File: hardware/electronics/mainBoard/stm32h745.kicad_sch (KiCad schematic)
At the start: 58 parts, among them SW1 PTS810, SW2 PTS810, U1 STM32H745ZIT6, U2 TCAN3403-Q1

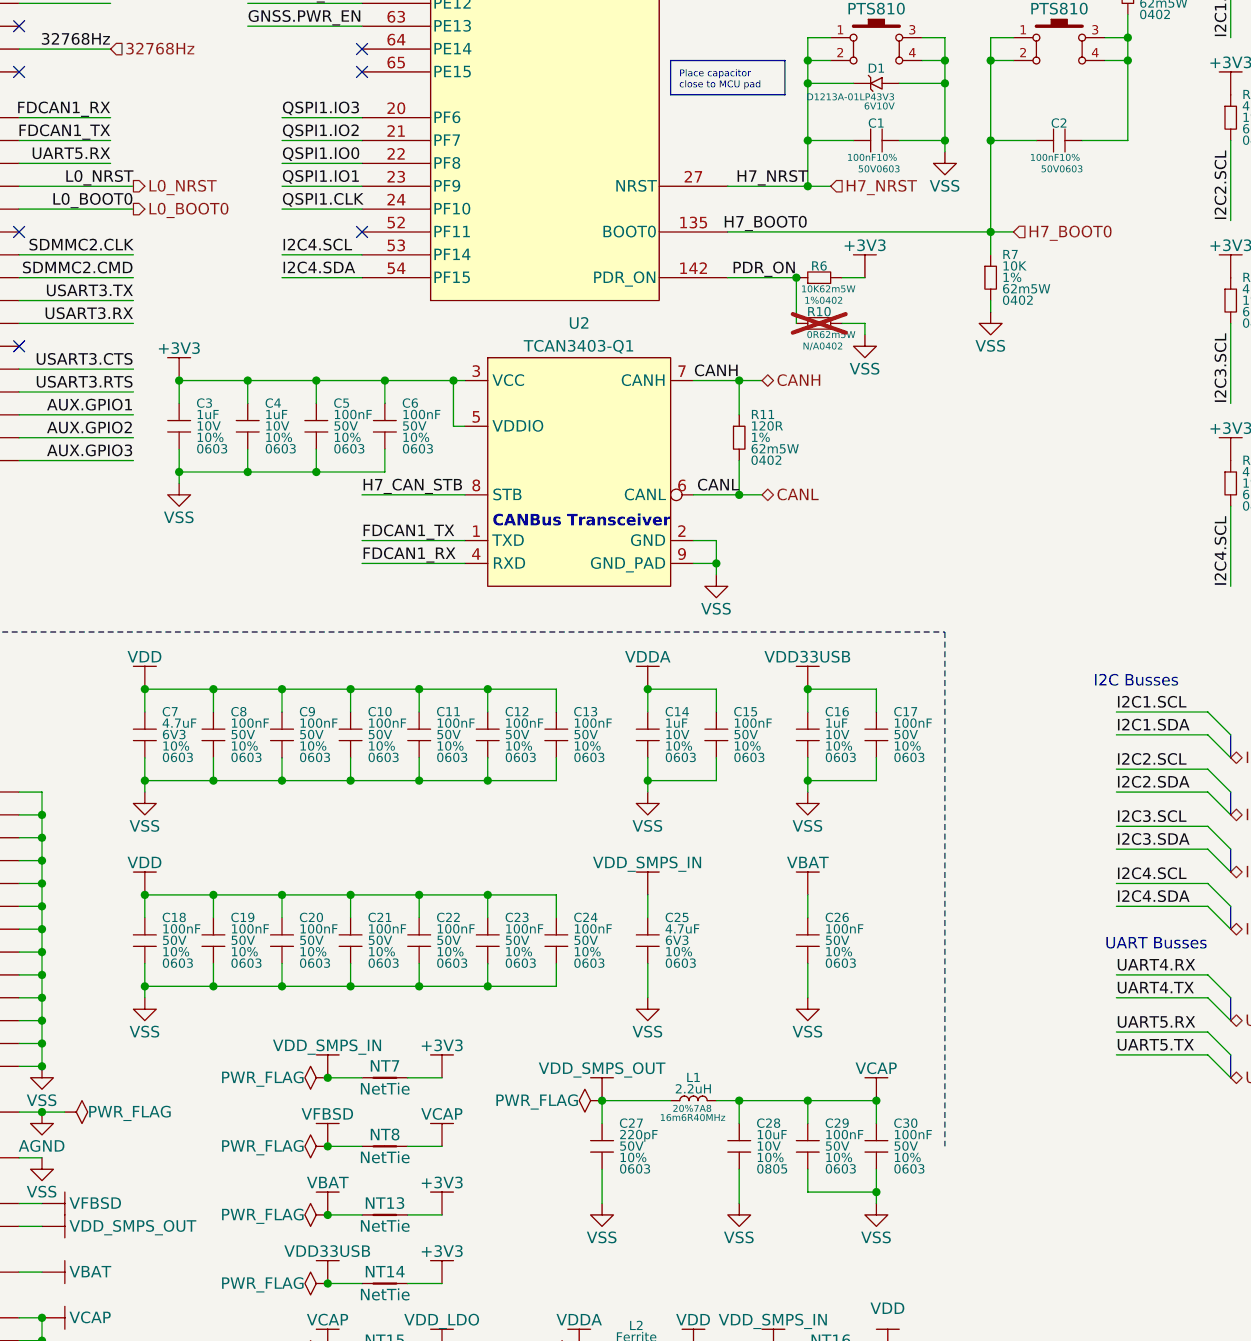
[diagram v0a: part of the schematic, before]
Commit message: updated capacitors
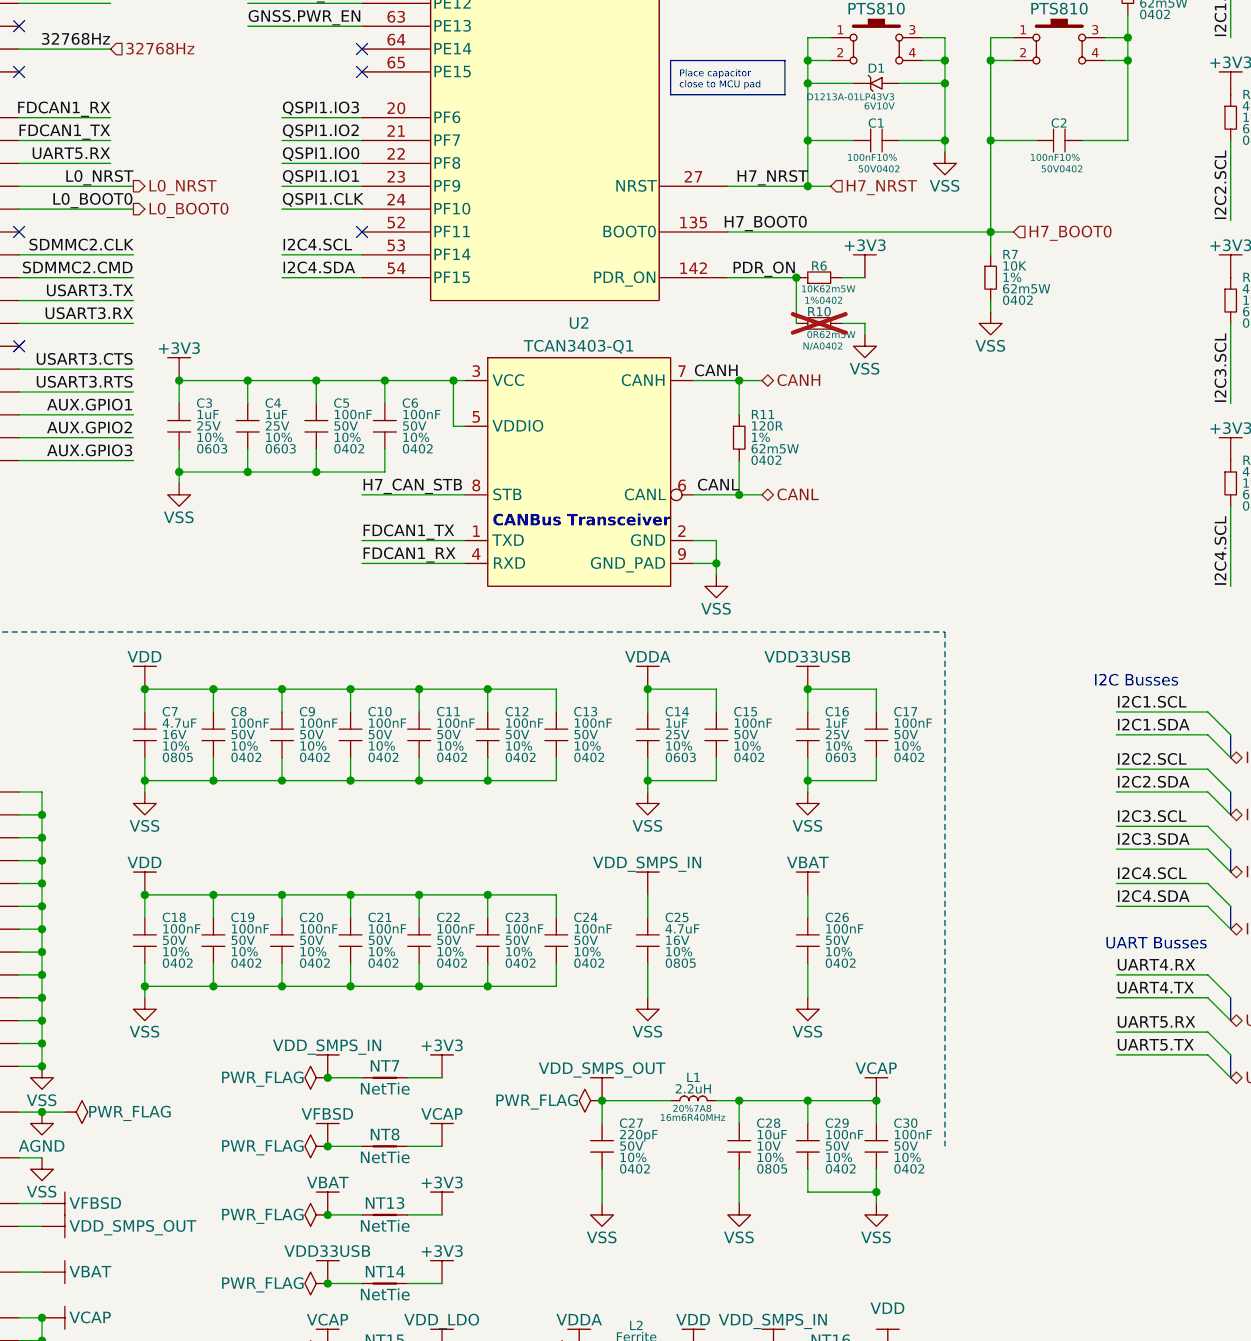
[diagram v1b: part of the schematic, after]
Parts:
- C1, C10, C11, C12, C13, C15, C17, C18, C19, C2, C20, C21, C22, C23, C24, C26, C29, C30, C5, C6, C8, C9: DKPN 478-KAM15AR71H104KTCT-ND -> 490-GRT155R71H104KE01DCT-ND; MPN 06035C104K4T2A -> GRT155R71H104KE01D; Manufacturer KYOCERA AVX -> Murata Electronics; Package 0603 -> 0402
- C14, C16, C3, C4: DKPN 478-KAM15AR71A105KTCT-ND -> 490-GRT188R71E105KE13DCT-ND; MPN KAM15AR71A105KT -> GRT188R71E105KE13D; Manufacturer KYOCERA AVX -> Murata Electronics; Voltage Rating 10V -> 25V
- C25, C7: DKPN 478-KAM15CR70J475KTCT-ND -> 490-GRT21BR71C475KE13LCT-ND; MPN KAM15CR70J475KT -> GRT21BR71C475KE13L; Manufacturer KYOCERA AVX -> Murata Electronics; Package 0603 -> 0805; Voltage Rating 6V3 -> 16V
- C27: DKPN 478-06035C221K4T2ACT-ND -> 490-GRT155R71H221KE01DCT-ND; MPN 06035C221K4T2A -> GRT155R71H221KE01D; Manufacturer KYOCERA AVX -> Murata Electronics; Package 0603 -> 0402
- C28: DKPN 478-KAM21AR71A106KUCT-ND -> 490-10674-1-ND; MPN KAM21AR71A106KU -> GCM21BR71A106KE22L; Manufacturer KYOCERA AVX -> Murata Electronics

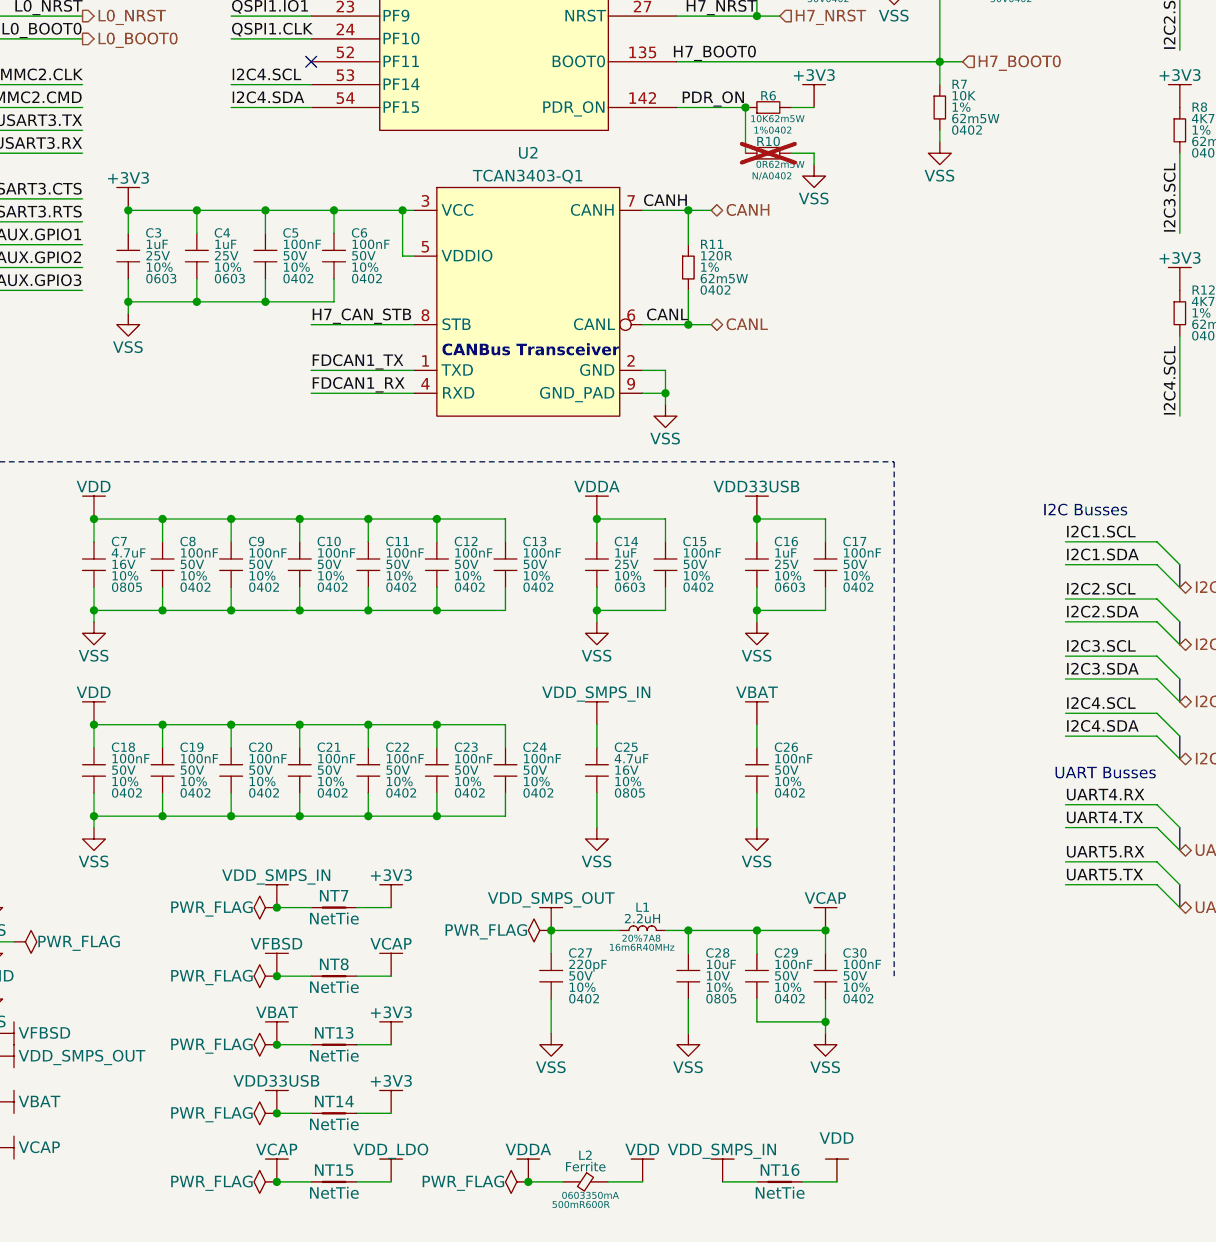
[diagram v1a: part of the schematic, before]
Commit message: added testpoints
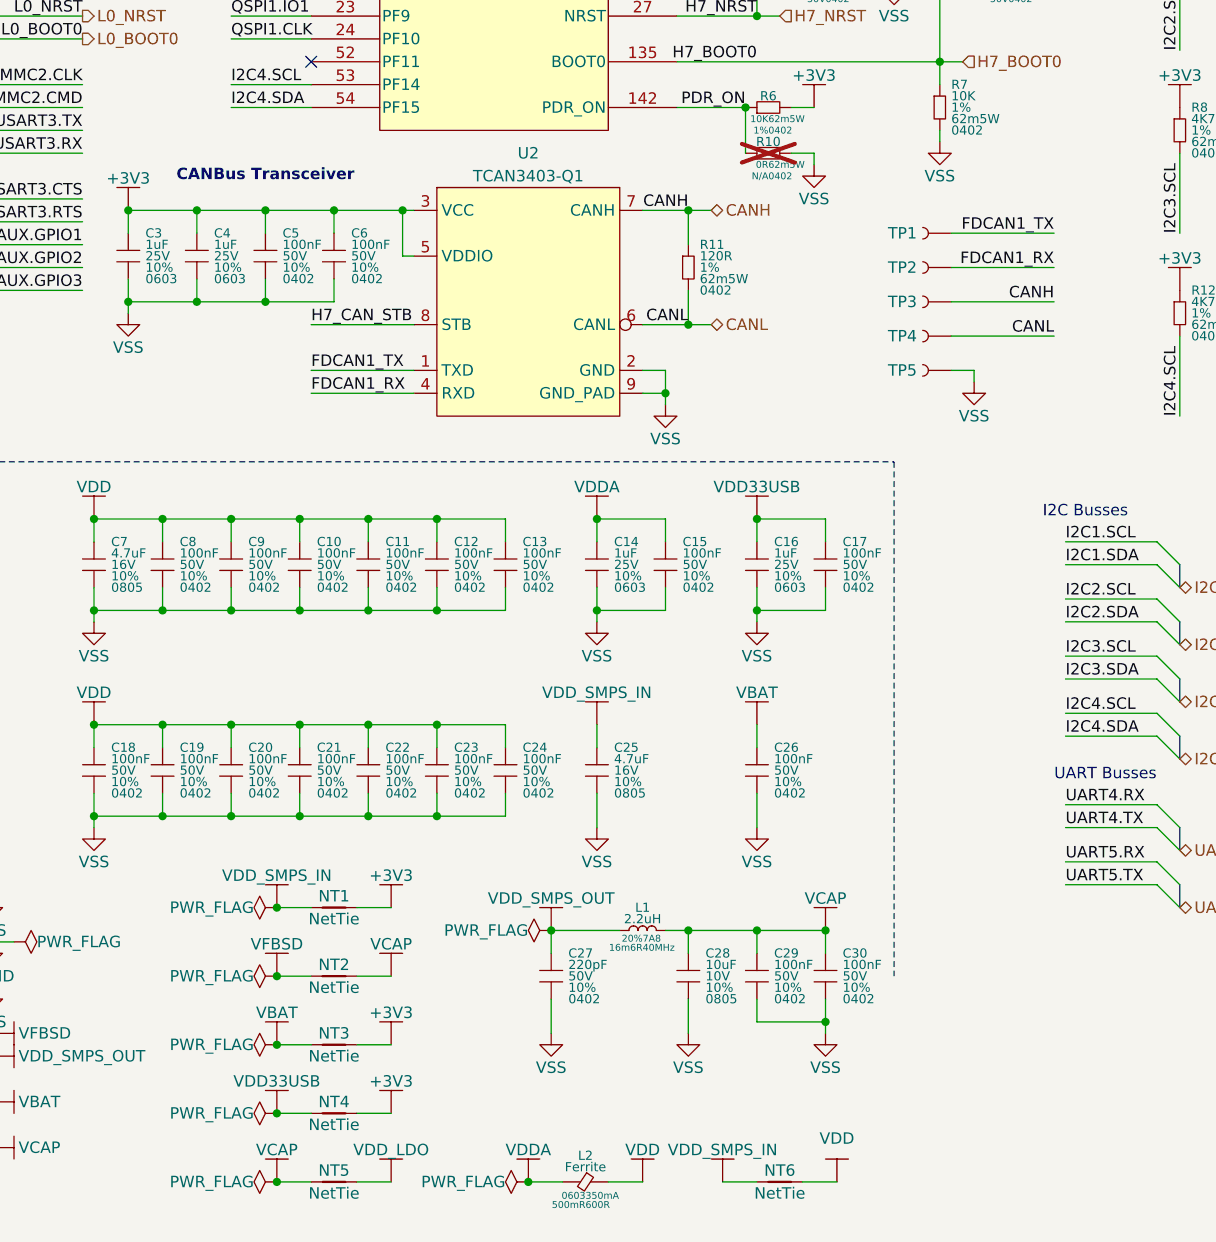
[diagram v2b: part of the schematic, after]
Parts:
- added TP1, TP2, TP3, TP4: ~, symbol lib_sch:Testpoint
- added TP5: RCWCTE, symbol lib_sch:Testpoint
- renumbered NT7 to NT1, NT8 to NT2, NT13 to NT3, NT14 to NT4, NT15 to NT5, NT16 to NT6
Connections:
- net CANH: now also TP3.1
- net CANL: now also TP4.1
- net FDCAN1_RX: now also TP2.1
- net FDCAN1_TX: now also TP1.1
- net VSS: now also TP5.1

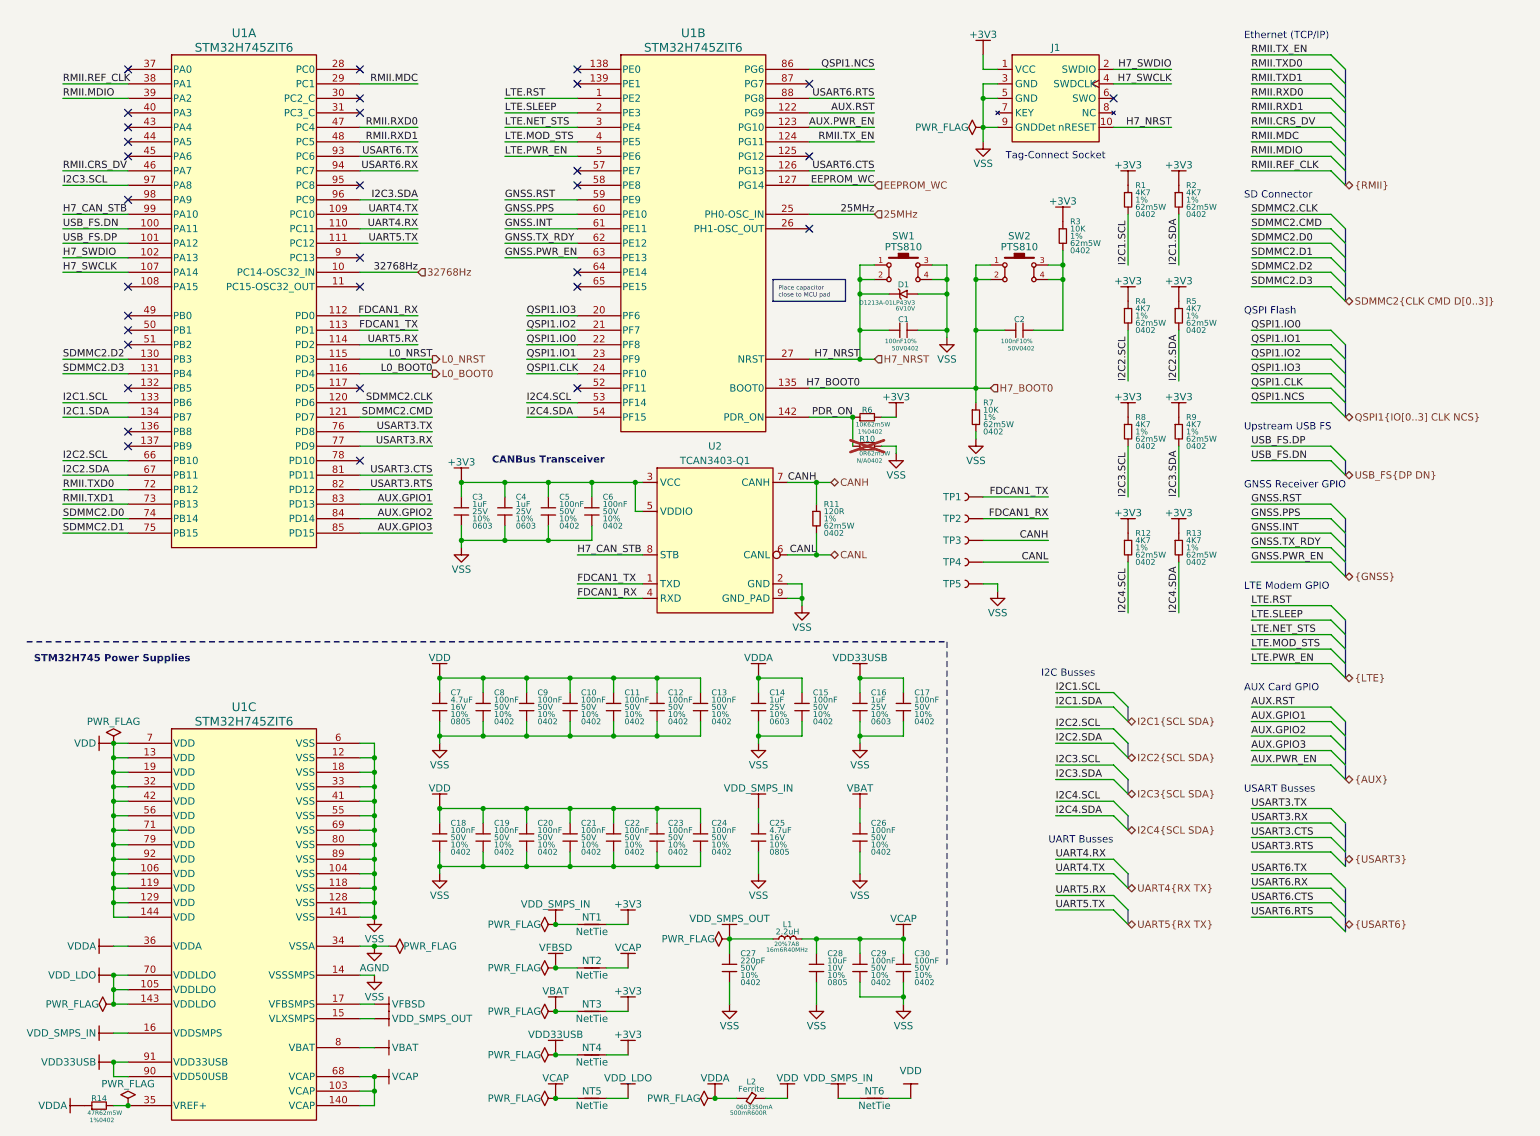
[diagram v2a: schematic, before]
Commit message: added usr LED
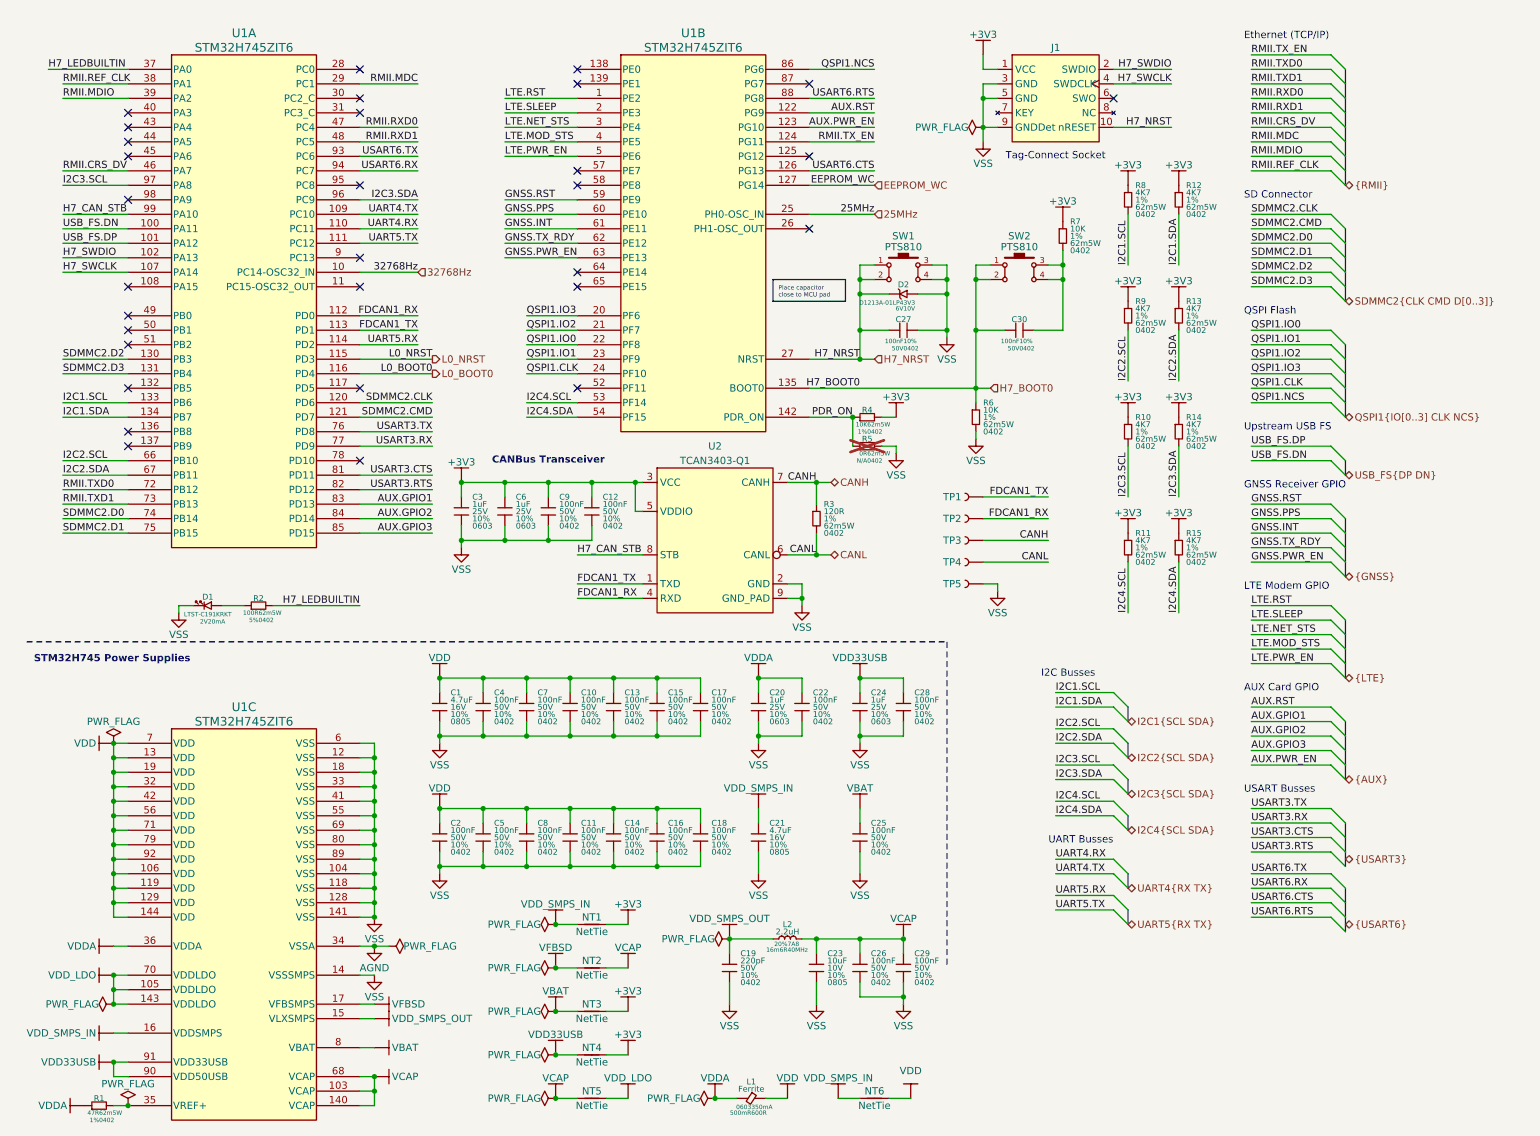
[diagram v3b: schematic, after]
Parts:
- added D1: LTST-C191KRKT, symbol lib_sch:LED_horizontal
- added R2: 100R, symbol lib_sch:R_horizontal
- renumbered C7 to C1, C21 to C11, C6 to C12, C11 to C13, C22 to C14, C12 to C15, C23 to C16, C13 to C17, C24 to C18, C27 to C19, C18 to C2, C14 to C20, C25 to C21, C15 to C22, C28 to C23, C16 to C24, C26 to C25, C29 to C26, C1 to C27, C17 to C28, C30 to C29, C2 to C30, C8 to C4, C19 to C5, C4 to C6, C9 to C7, C20 to C8, C5 to C9, D1 to D2, L2 to L1, L1 to L2, R14 to R1, R8 to R10, R12 to R11, R2 to R12, R5 to R13, R9 to R14, R13 to R15, R11 to R3, R6 to R4, R10 to R5, R7 to R6, R3 to R7, R1 to R8, R4 to R9
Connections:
- net VSS: now also D1.2
- net H7_LEDBUILTIN: now reaches U1.37 (PA0)
- net H7_LEDBUILTIN: now also R2.2
- new net: D1.1, R2.1
- no-connect marks 32 -> 31
